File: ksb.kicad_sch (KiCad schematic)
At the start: 19 parts, among them J10 Conn_01x02, J11 Conn_02x08_Top_Bottom, J12 Conn_02x08_Top_Bottom, J13 Conn_01x02, J4 Conn_02x08_Top_Bottom, J5 Conn_02x08_Top_Bottom, J6 Conn_02x16_Top_Bottom, J7 Conn_02x08_Top_Bottom, J9 Conn_01x02

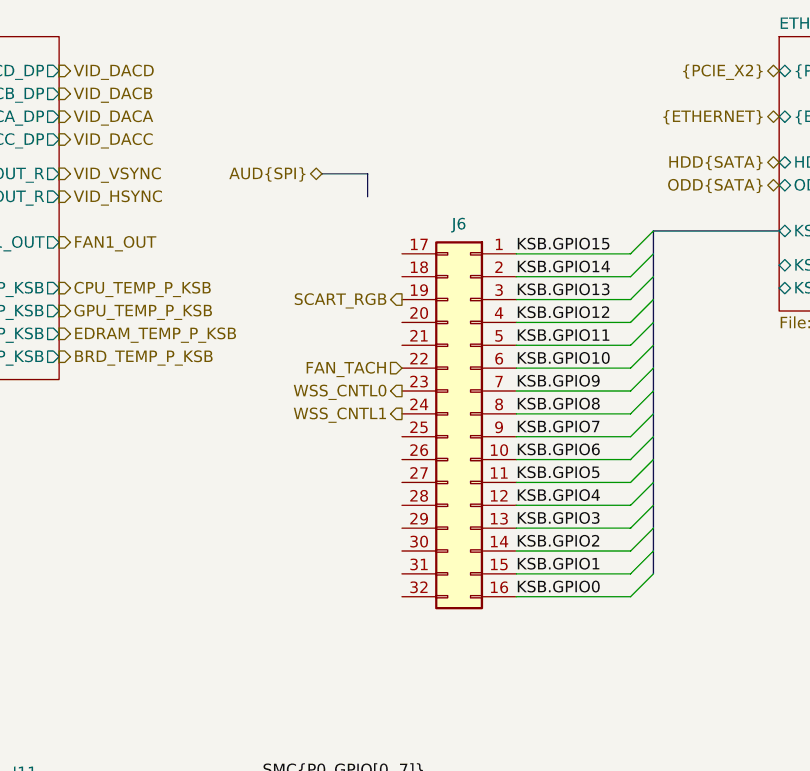
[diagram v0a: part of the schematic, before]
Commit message: Add VRAM schematic
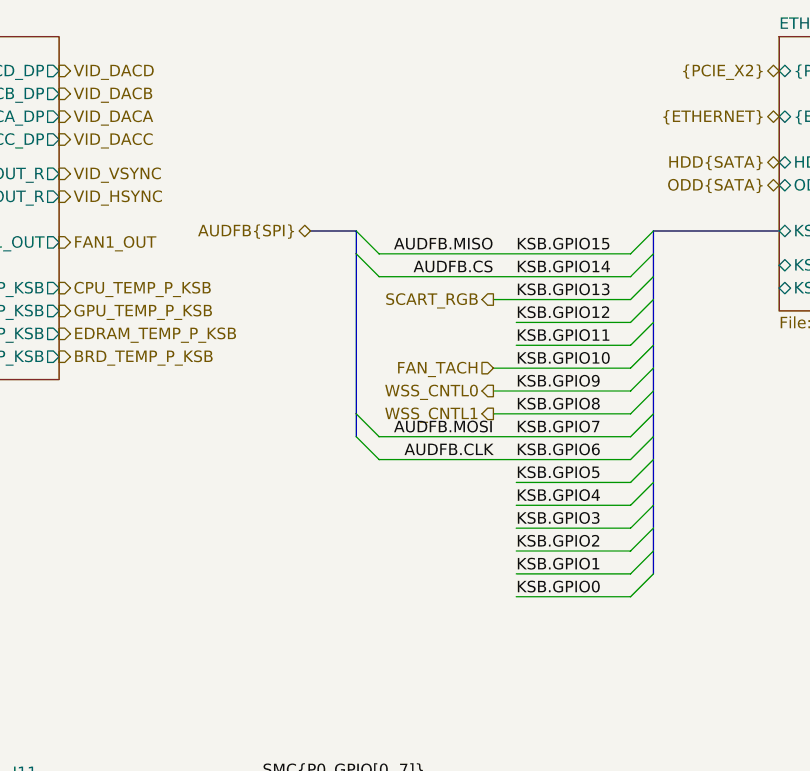
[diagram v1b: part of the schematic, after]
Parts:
- removed J6: Conn_02x16_Top_Bottom, symbol Connector_Generic:Conn_02x16_Top_Bottom

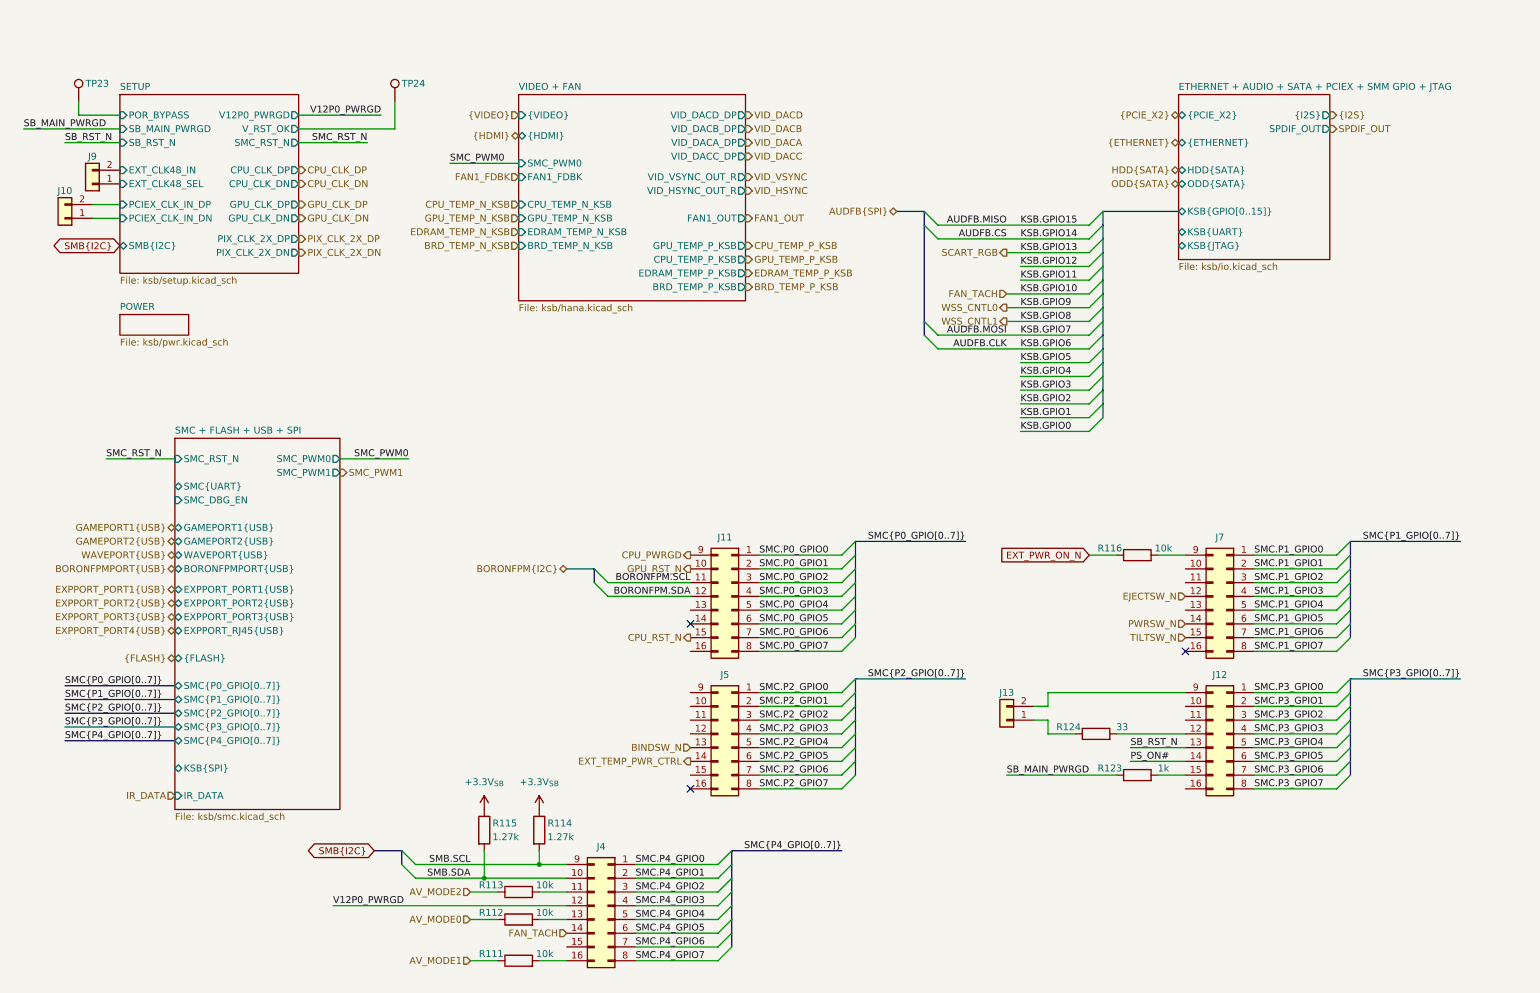
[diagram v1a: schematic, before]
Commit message: Cleanup, SMC GPIO connections and Temperature sensing
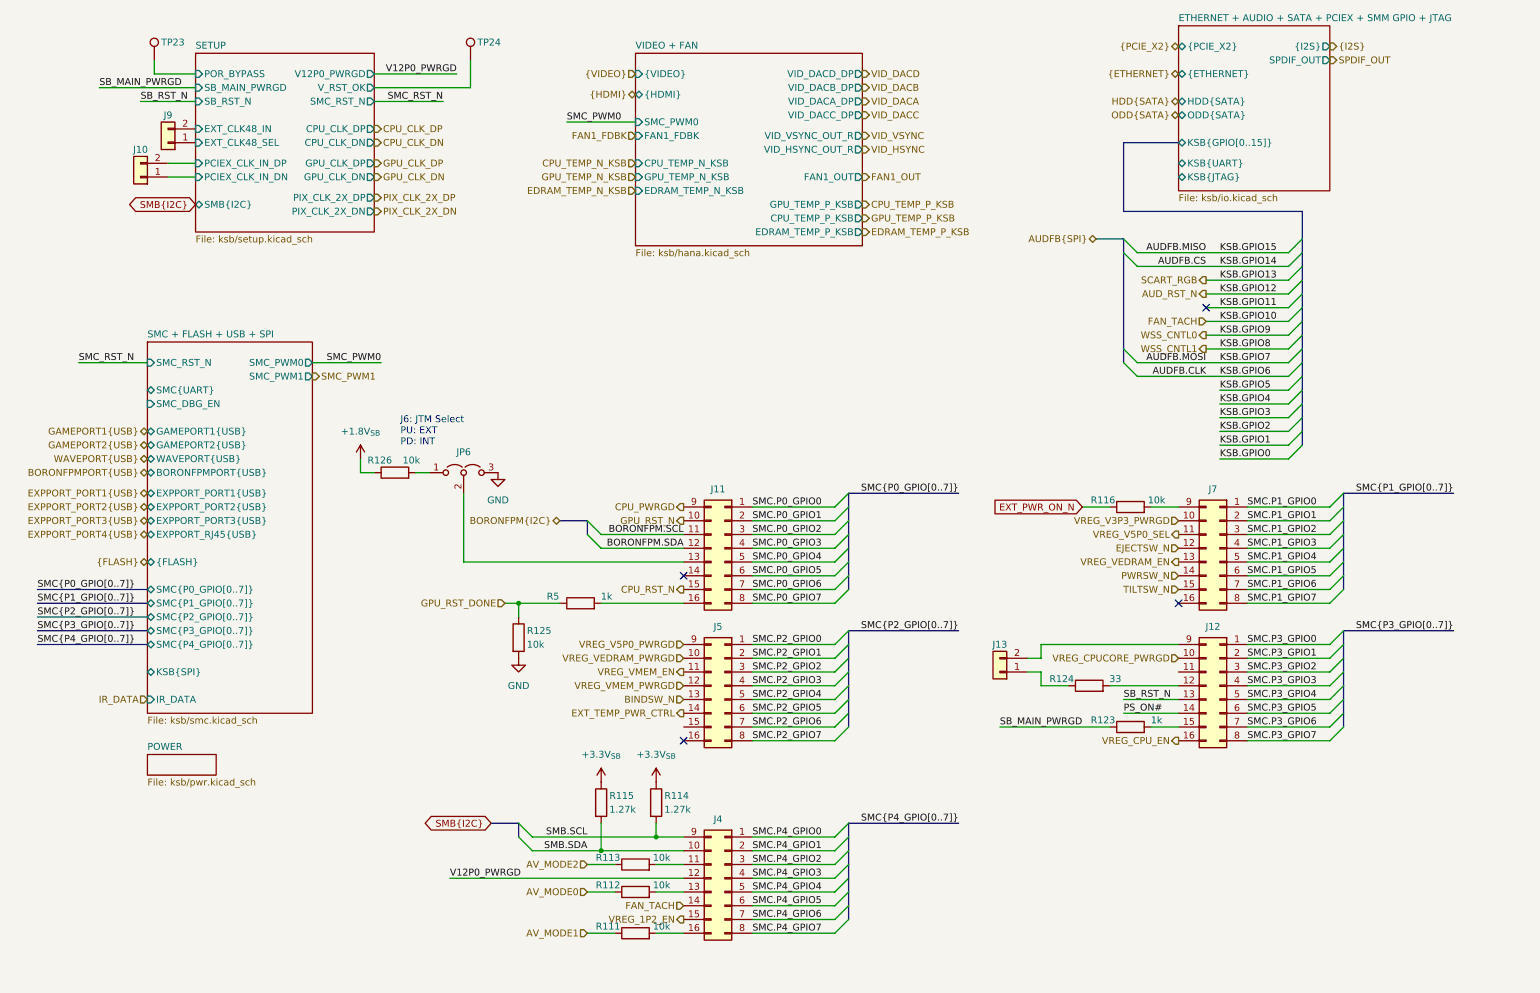
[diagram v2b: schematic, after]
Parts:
- added JP6: Jumper_3_Open, TestPoint:TestPoint_2Pads_Pitch5.08mm_Drill1.3mm, symbol Jumper:Jumper_3_Open
- added R125, R126: 10k, symbol Device:R
- added R5: 1k, symbol Device:R
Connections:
- net VREG_CPUCORE_PWRGD: now reaches J12.10 (Pin_10)
- net VREG_CPU_EN: now reaches J12.16 (Pin_16)
- net at J11.13 (Pin_13): now also JP6.2 (C)
- net at J11.16 (Pin_16): now also R5.2
- net VREG_1P2_EN: now reaches J4.15 (Pin_15)
- net VREG_VEDRAM_PWRGD: now reaches J5.10 (Pin_10)
- net VREG_VMEM_EN: now reaches J5.11 (Pin_11)
- net VREG_VMEM_PWRGD: now reaches J5.12 (Pin_12)
- net VREG_V5P0_PWRGD: now reaches J5.9 (Pin_9)
- net VREG_V3P3_PWRGD: now reaches J7.10 (Pin_10)
- net VREG_V5P0_SEL: now reaches J7.11 (Pin_11)
- net VREG_VEDRAM_EN: now reaches J7.13 (Pin_13)
- new net: JP6.1 (A), R126.2
- new net +1.8V_{SB}: R126.1
- new net GND: JP6.3 (B), R125.2
- new net GPU_RST_DONE: R125.1, R5.1
- no-connect marks 3 -> 4
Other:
- sheet VIDEO + FAN ports: added none; removed BRD_TEMP_N_KSB, BRD_TEMP_P_KSB
- note added: "J6: JTM Select PU: EXT PD: INT"
- moved on the sheet: J10, J11, J12, J13, J4, J5, J7, J9, R111, R112, R113, R114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

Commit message: Internal Connectors
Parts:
- removed J13: Conn_01x02, symbol Connector_Generic:Conn_01x02
- removed JP6: Jumper_3_Open, TestPoint:TestPoint_2Pads_Pitch5.08mm_Drill1.3mm, symbol Jumper:Jumper_3_Open
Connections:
- net +1.8V_{SB} is gone; now on an unnamed net: R126.1
- net GND: now also R126.2
- net TRAY_STATUS: now reaches J12.9 (Pin_9)
- net TRAY_OPEN: now reaches R124.1
- net EXT_TEMP_PWR_CTRL: no longer names the net of J5.14 (Pin_14)
- no-connect marks 4 -> 5
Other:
- sheet SMC + FLASH + USB + SPI ports: added EXPPORT_PORT0{USB}; removed EXPPORT_RJ45{USB}
- note removed: "J6: JTM Select PU: EXT PD: INT"

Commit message: Cleanup & Debug I/O
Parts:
- removed J11, J12, J4, J5, J7: Conn_02x08_Top_Bottom, symbol Connector_Generic:Conn_02x08_Top_Bottom
- added D34: LED, symbol Device:LED
- added J7: Conn_02x03_Odd_Even, symbol Connector_Generic:Conn_02x03_Odd_Even
- added JP6: Jumper_3_Open, symbol Jumper:Jumper_3_Open
- added R179: 249, symbol Device:R
- added R180: 2k, symbol Device:R
- added U15: 74LVC1G14, symbol 74xGxx:74LVC1G14
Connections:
- net +3.3V_{SB}: now also JP6.1 (A)
- net GND: now also J7.6 (Pin_6), JP6.3 (B), U15.3 (GND)
- net SMC.P0_GPIO4: now also R126.1
- net SMC.P0_GPIO7: now also R5.2
- net SMC.P1_GPIO0: now also R116.2
- net SMC.P3_GPIO3: now also R124.2
- net SMC.P3_GPIO6: now also R123.2
- net SMC.P4_GPIO2: now also R113.2
- net SMC.P4_GPIO4: now also R112.2
- net SMC.P4_GPIO7: now also R111.2
- new net: JP6.2 (C), R180.1
- new net: R179.1, U15.4
- new net: D34.1 (K), R179.2
- new net +5V_{DUAL}: D34.2 (A), U15.5 (VCC)
- new net DBG_LED0: R180.2, U15.2
- new net KSB.TCK: J7.5 (Pin_5)
- new net KSB.TDI: J7.1 (Pin_1)
- new net KSB.TDO: J7.3 (Pin_3)
- new net KSB.TMS: J7.2 (Pin_2)
- new net KSB.TRST: J7.4 (Pin_4)
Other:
- moved on the sheet: J10, J9, R111, R112, R113, R114, R115, R116, R123, R124, R125, R126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

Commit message: Debug Connectors
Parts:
- removed J7: Conn_02x03_Odd_Even, symbol Connector_Generic:Conn_02x03_Odd_Even
- added J8: Conn_01x02, symbol Connector_Generic:Conn_01x02
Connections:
- net SMC.P0_GPIO4: now also J8.1 (Pin_1)
- net SMC.P0_GPIO5: now also J8.2 (Pin_2)
- no-connect marks 5 -> 3
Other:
- moved on the sheet: J10, J9, TP23, TP24

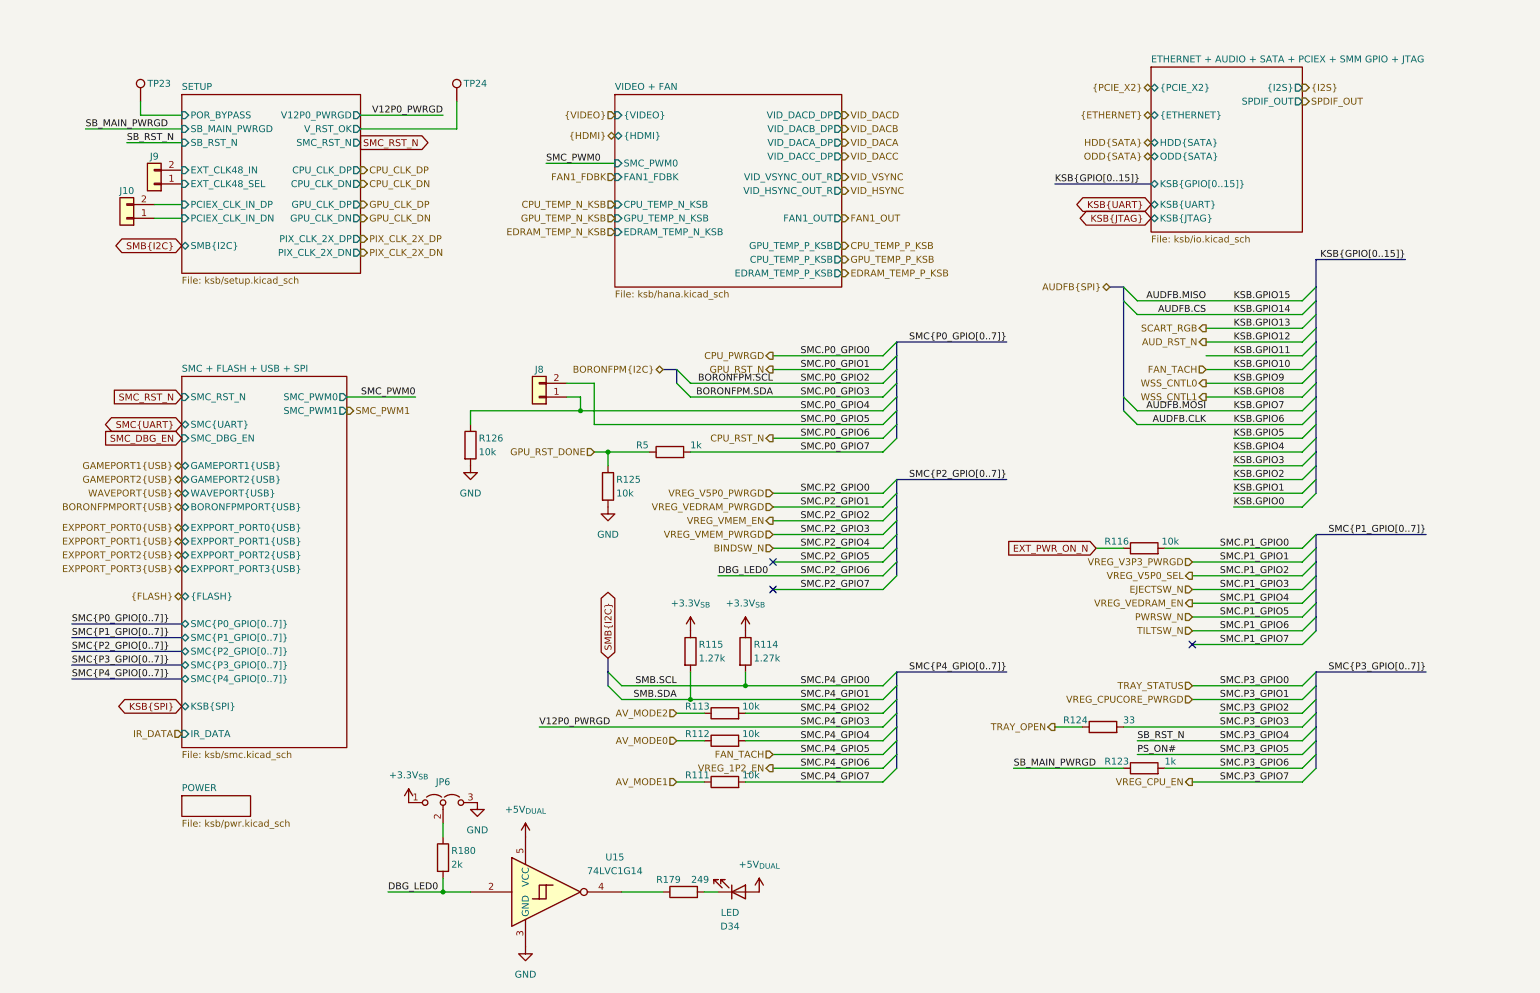
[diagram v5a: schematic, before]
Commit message: Nand Flash, Sata Connectors and removing (hopefully) unnecessary things
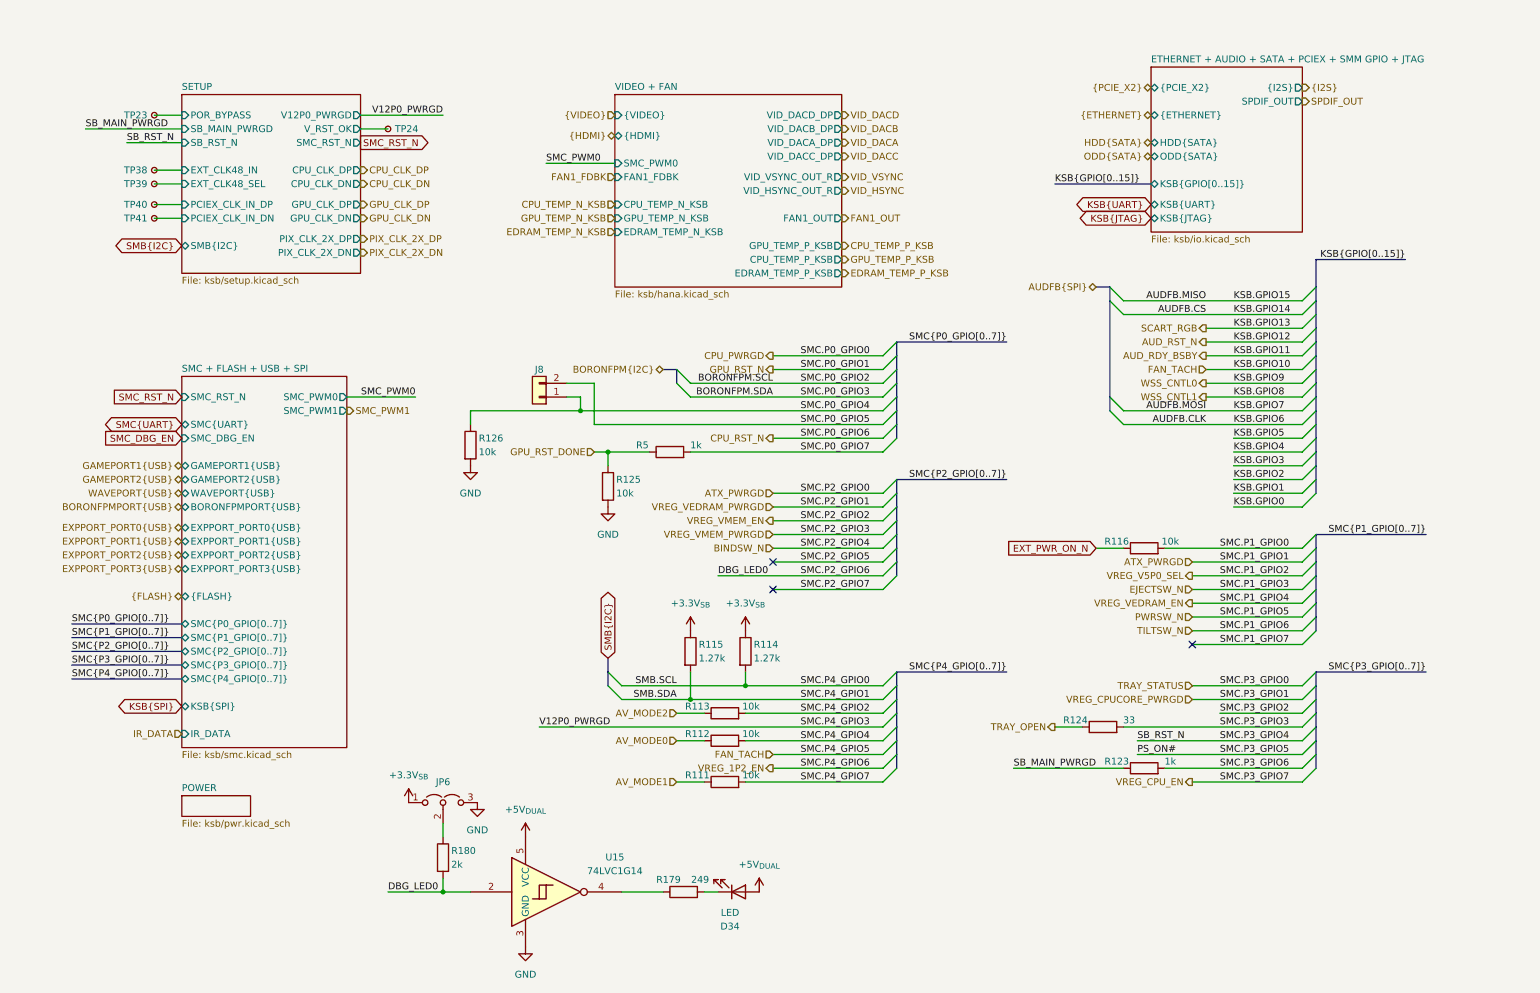
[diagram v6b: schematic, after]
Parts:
- removed J10, J9: Conn_01x02, symbol Connector_Generic:Conn_01x02
- removed TP23, TP24: TestPoint, symbol Connector:TestPoint
- added TP23, TP24, TP38, TP39, TP40, TP41: TestPoint_Small, symbol Connector:TestPoint_Small
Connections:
- net SETUP/EXT_CLK48_IN: now also TP38.1
- net SETUP/EXT_CLK48_SEL: now also TP39.1
- net SETUP/PCIEX_CLK_IN_DN: now also TP41.1
- net SETUP/PCIEX_CLK_IN_DP: now also TP40.1
- net SETUP/POR_BYPASS: now also TP23.1
- net SETUP/V_RST_OK: now also TP24.1
